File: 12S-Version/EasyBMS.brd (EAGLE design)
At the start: 49 x 100 mm, 149 parts, among them Q10 BSS84LT1G, Q11 BSS84LT1G, Q12 BSS84LT1G, Q13 BSS84LT1G, Q2 BSS84LT1G, Q3 BSS84LT1G, Q4 BSS84LT1G, Q5 BSS84LT1G, Q6 BSS84LT1G, Q7 BSS84LT1G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

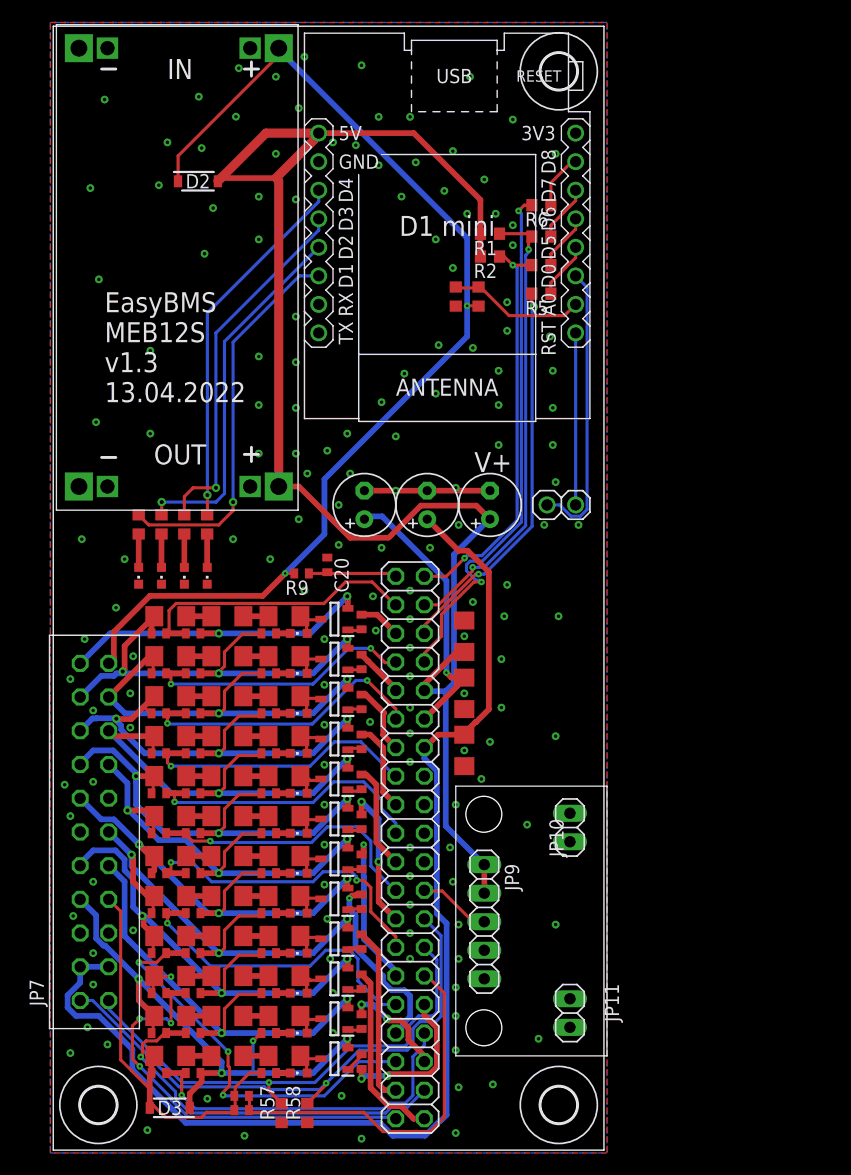
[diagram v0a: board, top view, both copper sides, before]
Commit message: removed diode, connected V+ and C12+, GND and BAT-, improved routing for C1 - C4
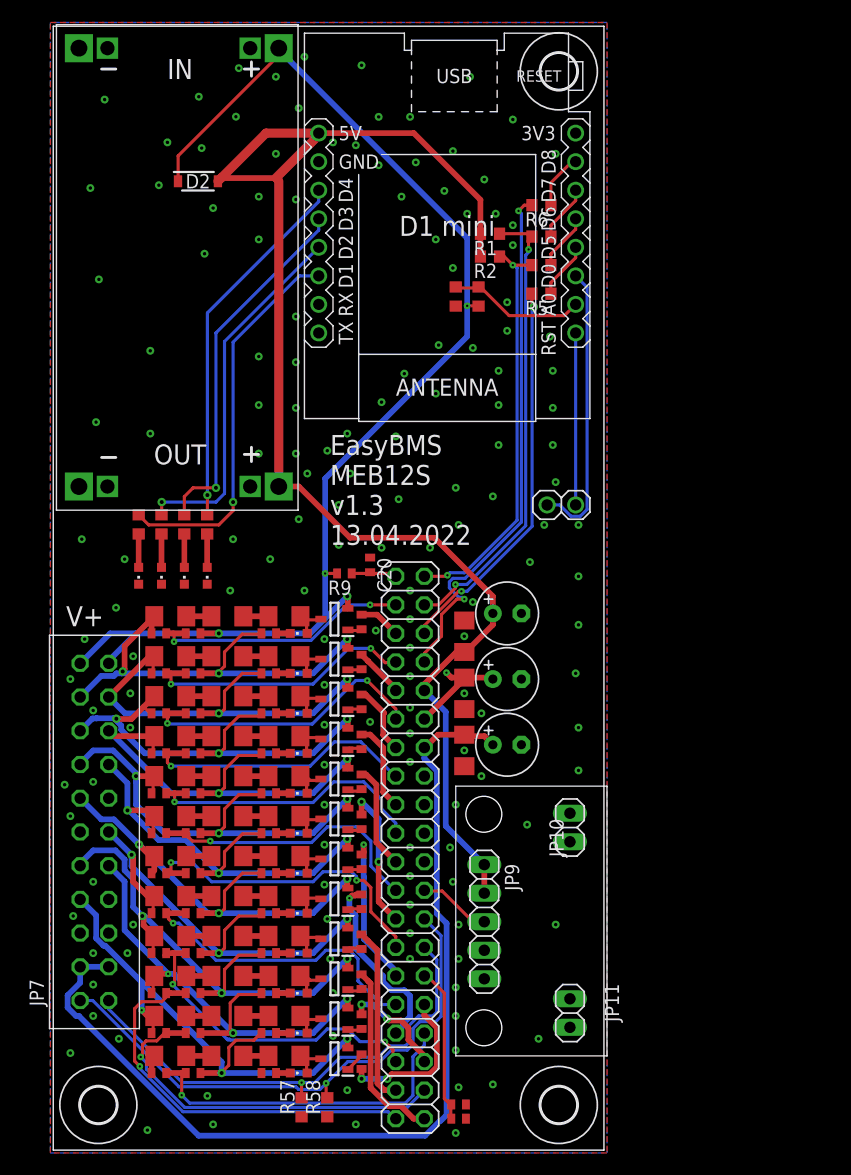
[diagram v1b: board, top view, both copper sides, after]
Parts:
- removed D3: SM4007PL-TP, SamacSys_Parts:SODFL3616X135N
- moved C2 22.5 mm to (40.4, 36.1), turned to 0 degrees
- moved C1 20.0 mm to (40.4, 41.9), turned to 0 degrees
- moved C5 19.4 mm to (36.1, 2.79), turned to 0 degrees
- moved R3 19.3 mm to (36.1, 4.06), turned to 0 degrees
- moved C3 9.77 mm to (40.4, 47.8), turned to 0 degrees
- moved R9 3.81 mm to (25.9, 51.3)
- moved C20 3.81 mm to (28.2, 52.1)
- moved R57 1.85 mm to (22.1, 3.81)
- moved R58 1.85 mm to (24.4, 3.81)
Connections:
- removed net C1-: C5.2, C6.2, D3.2, JP7.15_TOTAL-, R11.2, R3.2, R4.1
- removed net VIN: D2.1, JP7.1_TOTAL+, R15.2, R9.2, U$1.IN+
- net C1+: no longer D3.1
- net C12+: now also D2.1, JP7.1_TOTAL+, R15.2, R9.2, U$1.IN+
- net GND: now also C5.2, C6.2, JP7.15_TOTAL-, R11.2, R3.2, R4.1
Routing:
- net VIN: track 98.2 -> 0.00 mm, vias 2 -> 0
- net C12+: track 29.0 -> 113.1 mm, vias 2 -> 4
- net C1-: track 36.4 -> 0.00 mm
- net VREF2: track 107.4 -> 86.5 mm
- net C0: track 33.9 -> 14.5 mm
- net VREF1: track 24.9 -> 9.54 mm
- net 5VDC: track 136.9 -> 125.8 mm
- net GND: track 11.2 -> 2.13 mm, vias 158 -> 160
- net C4: track 36.6 -> 29.3 mm, vias 3 -> 2
- net V+: track 8.07 -> 4.26 mm
- net C12: track 26.0 -> 24.0 mm, vias 0 -> 2
- net C1+: track 48.9 -> 47.6 mm, vias 4 -> 3
- net C3: track 37.0 -> 35.7 mm, vias 3 -> 1
- net VTEMP2: track 50.7 -> 49.5 mm
- net VTEMP1: track 44.7 -> 43.7 mm
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
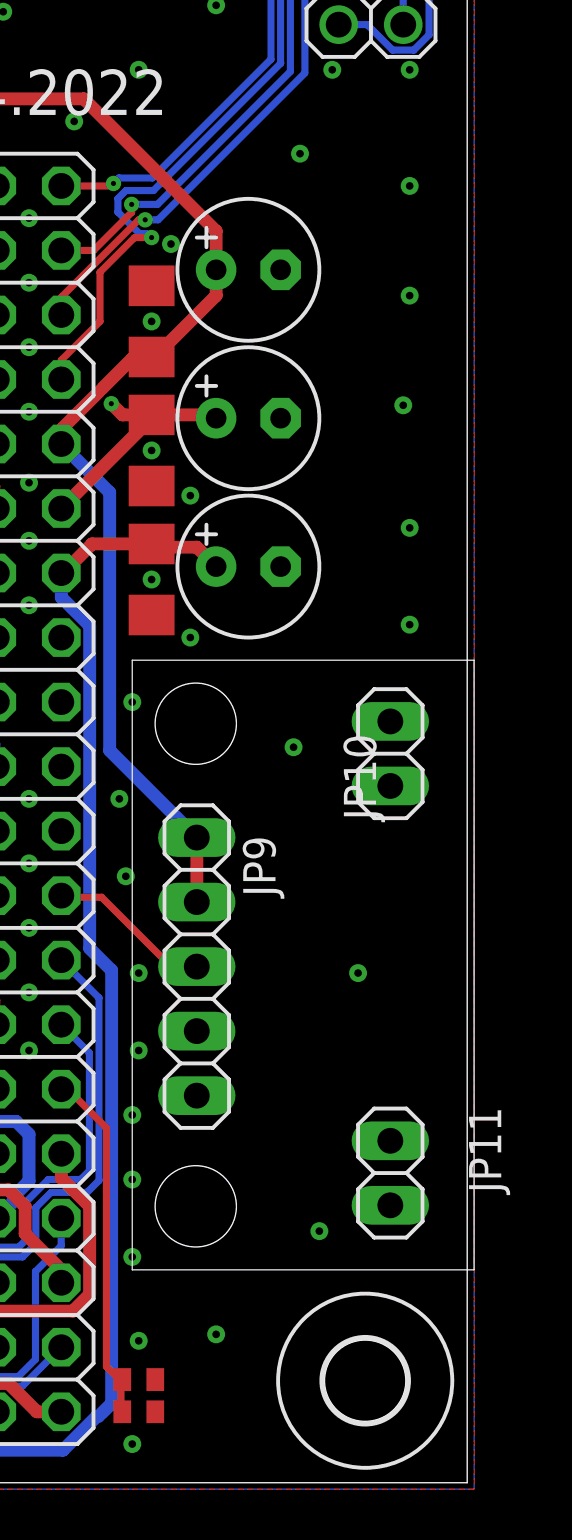
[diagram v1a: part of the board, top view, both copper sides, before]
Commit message: SMD pinheader added as a part
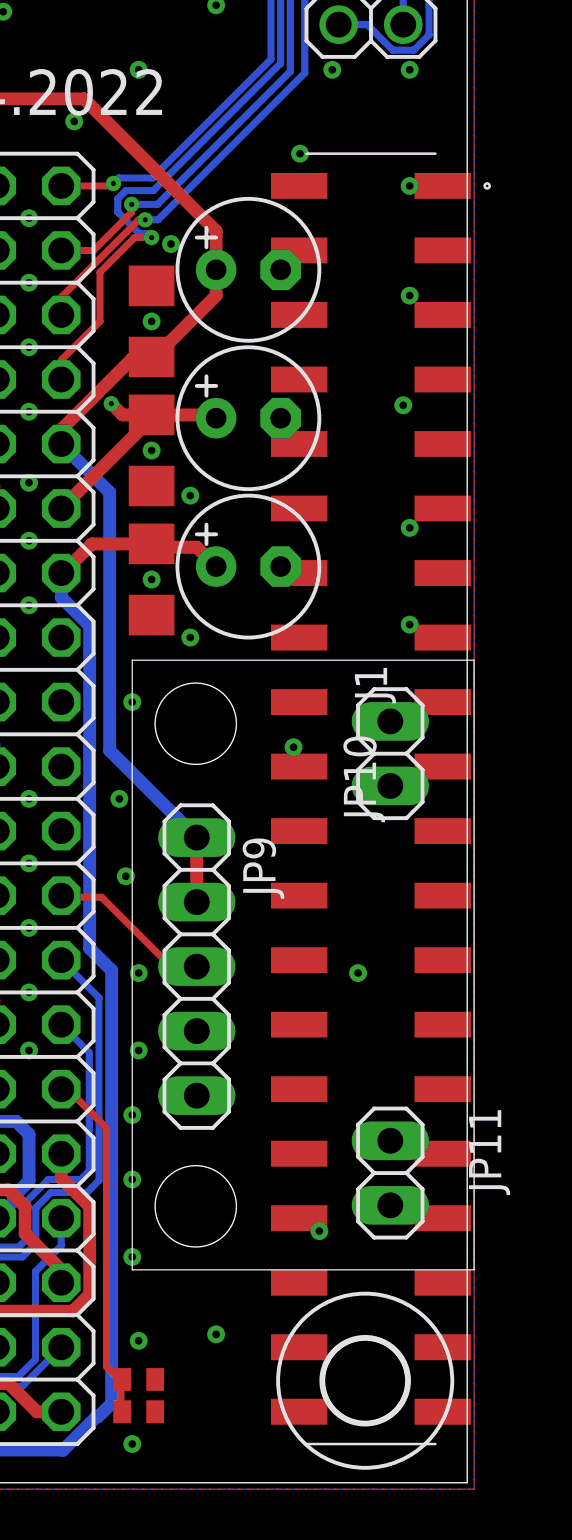
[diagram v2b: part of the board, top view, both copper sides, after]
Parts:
- added J1: SSM-120-SM-DV, SamacSys_Parts:SSM-120-XXX-DV
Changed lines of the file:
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@@
 <drawing>
 <settings>
-<setting alwaysvectorfont="yes"/>
+<setting alwaysvectorfont="no"/>
 <setting verticaltext="up"/>
 </settings>
@@
 <attribute name="VALUE" x="44.069" y="85.979" size="1.27" layer="27" rot="R180"/>
 </element>
+<element name="J1" library="SamacSys_Parts" package="SSM-120-XXX-DV" value="SSM-120-SM-DV" x="45.212" y="26.924" smashed="yes" rot="R90">
+<attribute name="DESCRIPTION" value="40 Position, Dual Row, Surface Mount PCB Socket Strip, 0.100&amp;quot; pitch" x="45.212" y="26.924" size="1.778" layer="27" rot="R90" display="off"/>
+<attribute name="HEIGHT" value="mm" x="45.212" y="26.924" size="1.778" layer="27" rot="R90" display="off"/>
+<attribute name="MANUFACTURER_NAME" value="SAMTEC" x="45.212" y="26.924" size="1.778" layer="27" rot="R90" display="off"/>
+<attribute name="MANUFACTURER_PART_NUMBER" value="SSM-120-SM-DV" x="45.212" y="26.924" size="1.778" layer="27" rot="R90" display="off"/>
+<attribute name="MOUSER_PART_NUMBER" value="" x="45.212" y="26.924" size="1.778" layer="27" rot="R90" display="off"/>
+<attribute name="MOUSER_PRICE-STOCK" value="" x="45.212" y="26.924" size="1.778" layer="27" rot="R90" display="off"/>
+<attribute name="NAME" x="45.212" y="31.496" size="1.27" layer="25" rot="R90" align="center"/>
+<attribute name="VALUE" x="45.212" y="26.924" size="1.27" layer="27" rot="R90" align="center"/>
+</element>
 </elements>

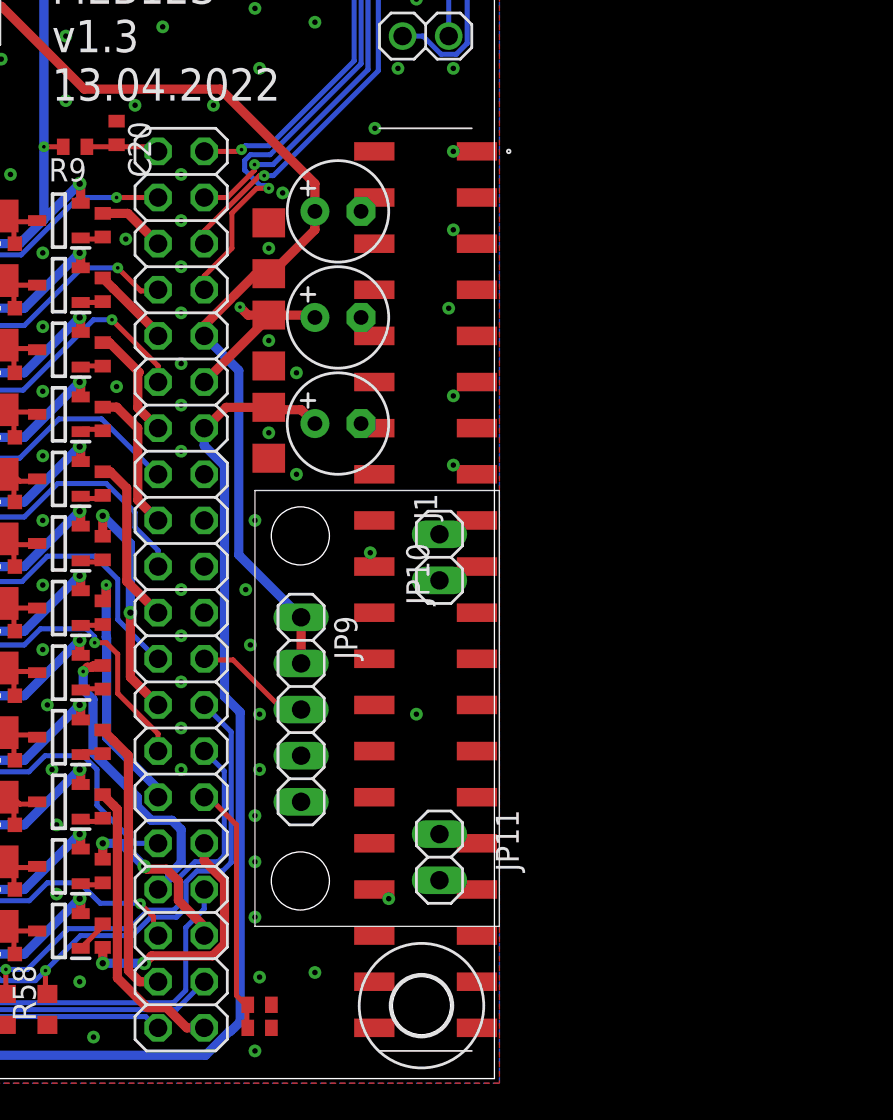
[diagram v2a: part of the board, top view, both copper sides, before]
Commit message: SMD pinheader swaped but not placed
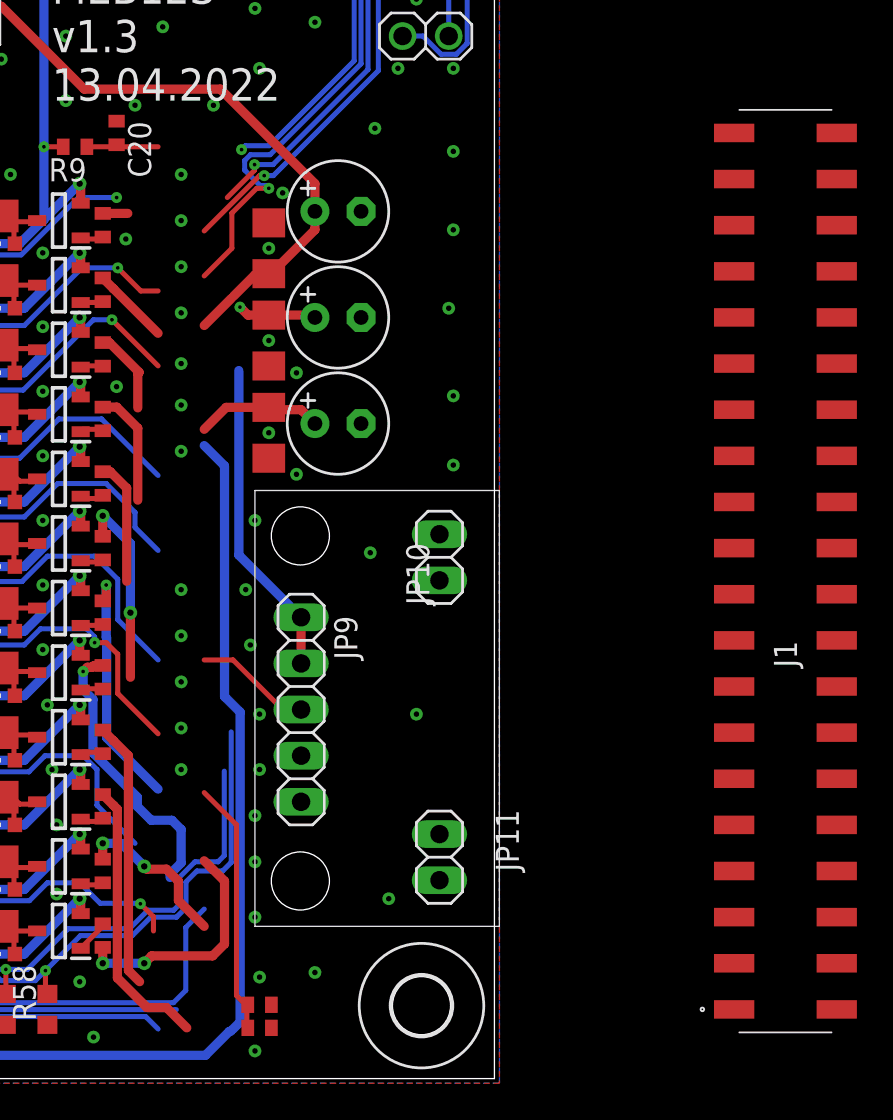
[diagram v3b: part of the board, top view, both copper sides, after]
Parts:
- removed JP5: (no value), pinhead:2X20
- moved J1 19.8 mm to (65.0, 27.9), turned to 270 degrees
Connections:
- net 5VDC: now also J1.32; no longer JP5.10
- net C0: now also J1.12; no longer JP5.30
- net C1: now also J1.8; no longer JP5.34
- net C10: now also J1.29; no longer JP5.11
- net C11: now also J1.33; no longer JP5.7
- net C12: now also J1.37; no longer JP5.3
- net C2: now also J1.4; no longer JP5.38
- net C3: now also J1.1; no longer JP5.39
- net C4: now also J1.5; no longer JP5.35
- net C5: now also J1.9; no longer JP5.31
- net C6: now also J1.13; no longer JP5.27
- net C7: now also J1.17; no longer JP5.23
- net C8: now also J1.21; no longer JP5.19
- net C9: now also J1.25; no longer JP5.15
- net CSB: now also J1.34; no longer JP5.8
- net GND: now also J1.24, J1.26; no longer JP5.16, JP5.18
- net GPIO4: now also J1.20; no longer JP5.22
- net GPIO5: now also J1.22; no longer JP5.20
- net ISIGNAL: now also J1.18; no longer JP5.24
- net MISO: now also J1.40; no longer JP5.2
- net MOSI: now also J1.38; no longer JP5.4
- net S1: now also J1.10; no longer JP5.32
- net S10: now also J1.27; no longer JP5.13
- net S11: now also J1.31; no longer JP5.9
- net S12: now also J1.35; no longer JP5.5
- net S2: now also J1.6; no longer JP5.36
- net S3: now also J1.2; no longer JP5.40
- net S4: now also J1.3; no longer JP5.37
- net S5: now also J1.7; no longer JP5.33
- net S6: now also J1.11; no longer JP5.29
- net S7: now also J1.15; no longer JP5.25
- net S8: now also J1.19; no longer JP5.21
- net S9: now also J1.23; no longer JP5.17
- net SCK: now also J1.36; no longer JP5.6
- net V+: now also J1.39; no longer JP5.1
- net VREF1: now also J1.30; no longer JP5.12
- net VREF2: now also J1.28; no longer JP5.14
- net VTEMP1: now also J1.14; no longer JP5.28
- net VTEMP2: now also J1.16; no longer JP5.26
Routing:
- net VREF1: track 9.54 -> 4.69 mm
- net 5VDC: track 125.8 -> 122.4 mm
- net S8: track 9.27 -> 6.83 mm
- net S12: track 3.74 -> 1.38 mm
- net C12: track 24.0 -> 21.7 mm
- net C2: track 33.5 -> 31.3 mm
- net S7: track 12.8 -> 10.6 mm
- net VTEMP2: track 49.5 -> 47.4 mm
- net MISO: track 36.4 -> 34.5 mm
- net S10: track 6.25 -> 4.67 mm
- net S9: track 7.95 -> 6.37 mm
- net VTEMP1: track 43.7 -> 42.1 mm
- net C5: track 27.6 -> 26.3 mm
- net MOSI: track 41.1 -> 39.9 mm
- net C1: track 30.8 -> 29.8 mm
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
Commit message: traced ripped up
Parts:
- moved J1 32.8 mm to (32.3, 26.6)
- moved C1 5.16 mm to (45.5, 41.8)
- moved C2 5.16 mm to (45.5, 36.0)
- moved C3 5.16 mm to (45.5, 47.7)
- moved C19 4.40 mm to (40.9, 46.2)
- moved C18 4.39 mm to (40.9, 41.1)
- moved C4 4.39 mm to (40.9, 35.9)
- moved C5 3.51 mm to (39.0, 4.70)
- moved R3 3.40 mm to (39.0, 5.77)
- moved C20 0.77 mm to (28.0, 52.8)
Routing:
- net VREF2: track 85.4 -> 23.3 mm
- net 5VDC: track 122.4 -> 79.2 mm
- net C1: track 29.8 -> 4.72 mm
- net C2: track 31.3 -> 11.5 mm
- net C3: track 35.7 -> 16.4 mm
- net VTEMP2: track 47.4 -> 29.5 mm
- net VTEMP1: track 42.1 -> 26.3 mm
- net S3: track 15.4 -> 0.00 mm
- net S4: track 14.7 -> 0.00 mm
- net C0: track 14.2 -> 0.64 mm
- net S6: track 13.4 -> 0.05 mm, vias 1 -> 0
- net S1: track 13.1 -> 0.00 mm, vias 2 -> 0
- net S5: track 15.7 -> 4.70 mm
- net S7: track 10.6 -> 0.00 mm, vias 2 -> 0
- net CSB: track 46.8 -> 36.3 mm, vias 2 -> 1
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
